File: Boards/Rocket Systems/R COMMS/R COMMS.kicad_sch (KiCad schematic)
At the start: 47 parts, among them IC1 NSVT30010MXV6T1G, IC2 NSVT30010MXV6T1G, J2 22022065, J4 MEM2061-01-188-00-A_REVA, J6 SMA_CONNECTOR, J7 SMA_CONNECTOR, J9 Conn_01x04_Socket, U3 SX1280IMLTRT, U4 NRF21540-QDAA-R, U6 MAX485CSA+T

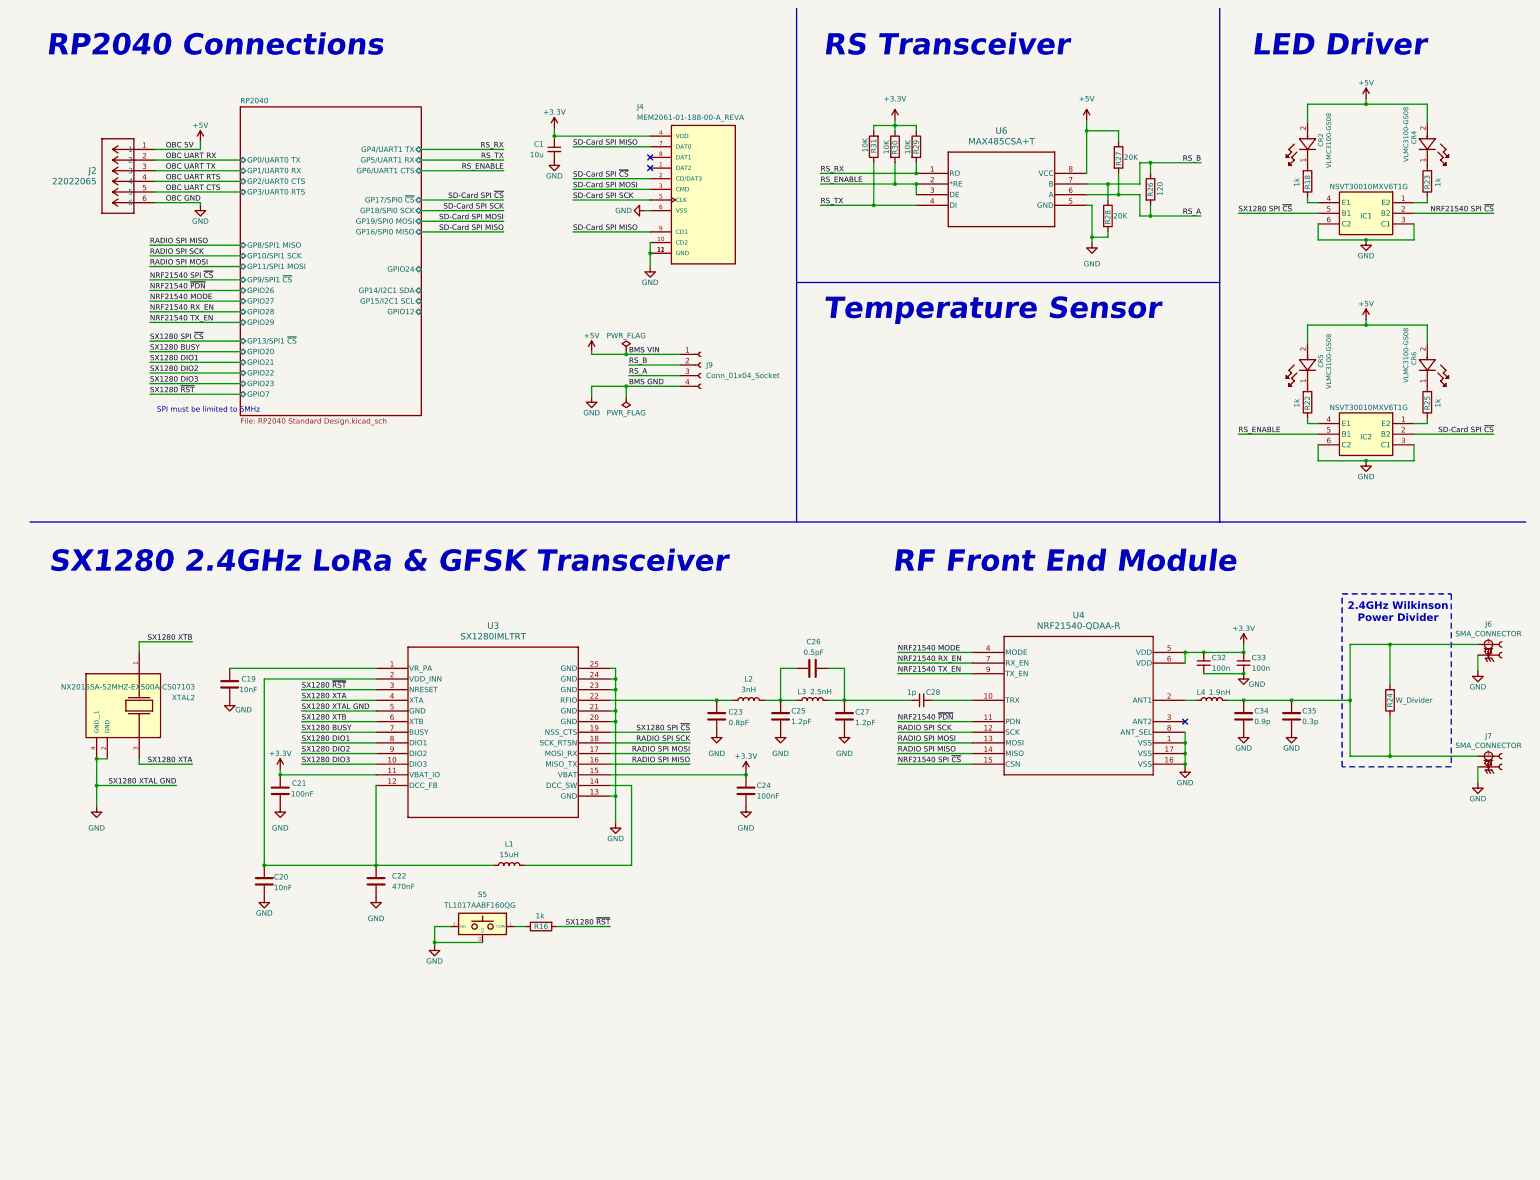
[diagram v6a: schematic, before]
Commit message: Communication System final Schematic Update
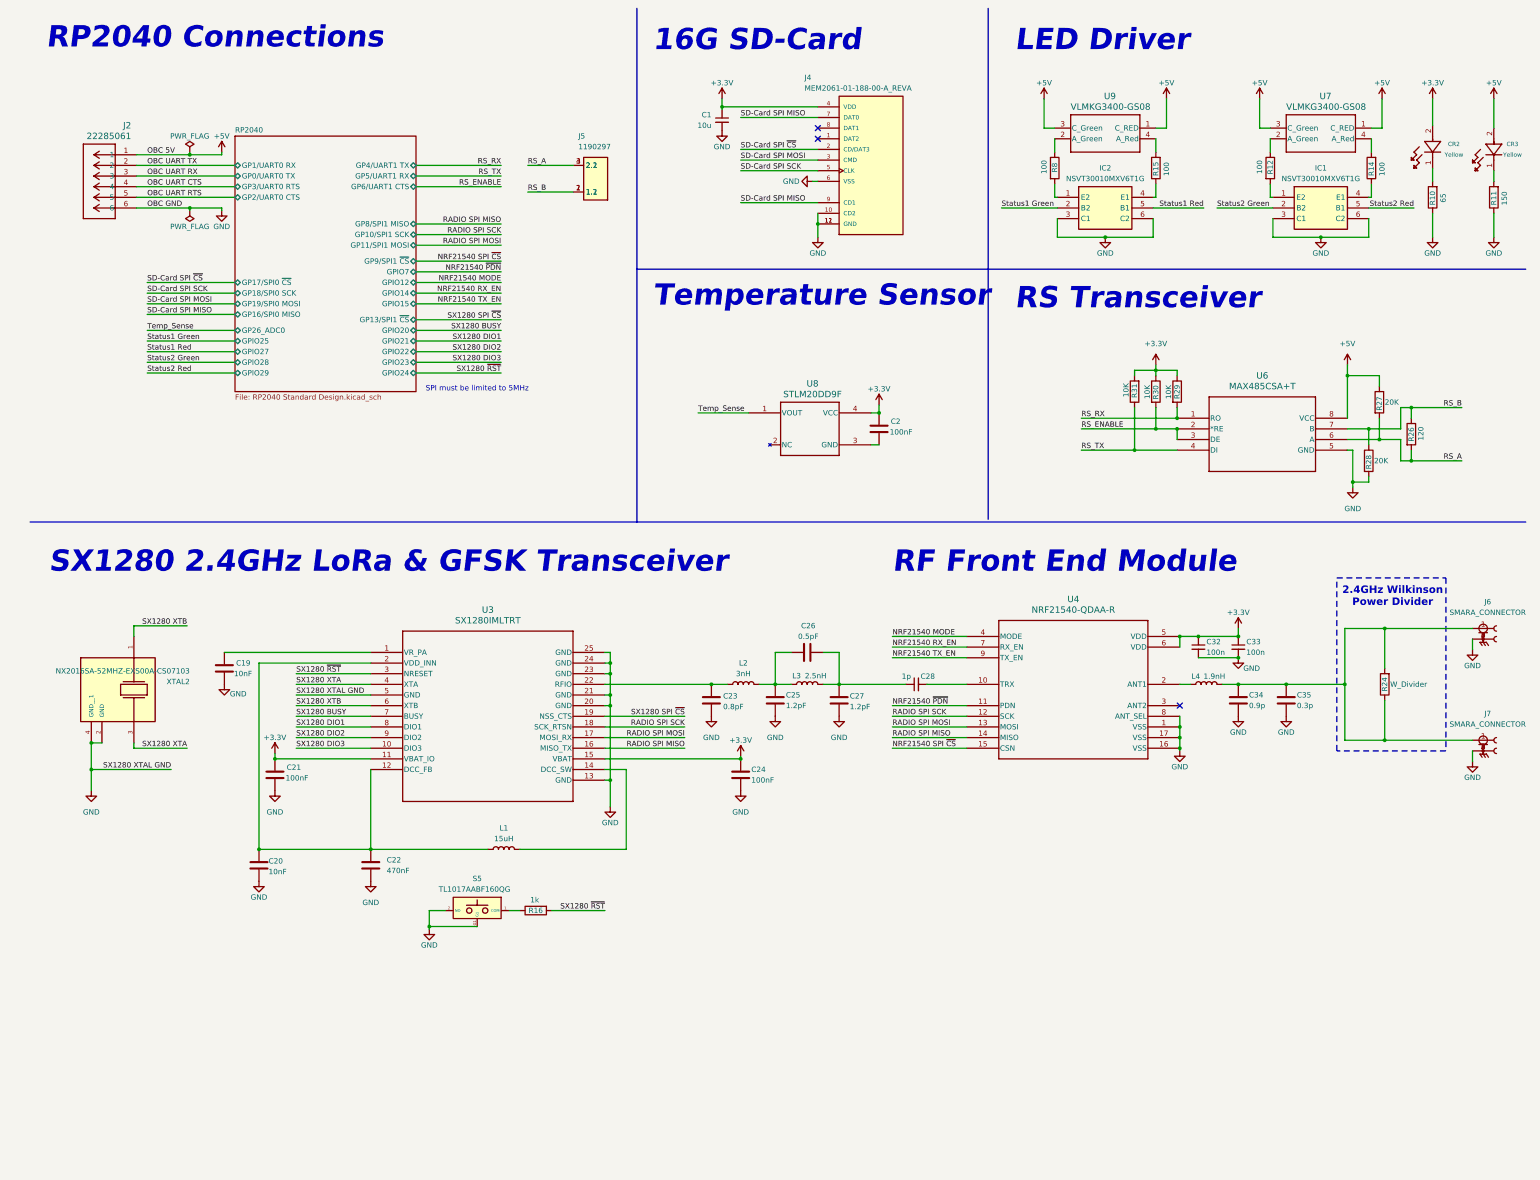
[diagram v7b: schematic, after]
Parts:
- removed CR2, CR4, CR5, CR6: VLMC3100-GS08, LED-Green_VLMC3100-GS08:LED_PLCC_VSMB, symbol GreenLED__VLMC3100-GS08:VLMC3100-GS08
- removed J2: 22022065, CONN_SA-4455_06_TE_MOL, symbol CONN_SA-4455_06_TE_MOL:22022065
- removed J6: SMA_CONNECTOR, SMA_CONNECTOR:LPRS_SMA_CONNECTOR, symbol SMA_CONNECTOR:SMA_CONNECTOR
- removed J7: SMA_CONNECTOR, Inductor-0805:Inductor_0805, symbol SMA_CONNECTOR:SMA_CONNECTOR
- removed J9: Conn_01x04_Socket, symbol Connector:Conn_01x04_Socket
- removed R18, R22, R23, R25: 1k, Resistor-0402:RES_0402, symbol Device:R
- added C2: 100nF, Capacitor-0402:Capacitor_0402, symbol Device:C
- added CR2, CR3: VLMY1300-GS08, LED-Yellow_VLMY1300-GS08:LED_VISHAY_VLMX1300_VIS, symbol VLMY1300-GS08:VLMY1300-GS08
- added J2: 22285061, CONN Male Header:CONN_SD-42375-001_M320_06_MOL, symbol PinCon_22285061:22285061
- added J5: 1190297, LPT Conn 2 Entradas:1190297, symbol 1190297:1190297
- added J6, J7: SMARA_CONNECTOR, SMARACONNECTOR, symbol SMARA_CONNECTOR:SMARA_CONNECTOR
- added R10: 65, Resistor-0402:RES_0402, symbol Device:R
- added R11: 150, Resistor-0402:RES_0402, symbol Device:R
- added R12, R14, R15, R8: 100, Resistor-0402:RES_0402, symbol Device:R
- added U7, U9: VLMKG3400-GS08, VLMKG3400-GS08:SMT_00-GS08_VIS, symbol VLMKG3400-GS08:VLMKG3400-GS08
- added U8: STLM20DD9F, STLM20DD9F:UDFN-4L_STM, symbol STLM20DD9F:STLM20DD9F
- C1: footprint (none) -> Capacitor-0805:Capacitor_0805
- IC1, IC2: footprint 2 PNP:SOTFL50P160X60-6N -> 2 PNP:SOT-563_1P3X1P7_ONS
- J4: footprint MEM2061-01-188-00-A_REVA:GCT_MEM2061-01-188-00-A_REVA -> SD-CARD_MEM2061-01-188-00-A:GCT_MEM2061-01-188-00-A_REVA
- L1: footprint Inductor-0805:IND_15uH_0805 -> Inductor-0805:Inductor_0805
- R24: footprint Resistor-0805:R_0805_5K1 -> Resistor-0805:RES_0805
- S5: footprint TL1017AABF160QG -> E-Switch_Small:TL1017AABF160QG
- U3: footprint QFN24_4X4_SEM -> SX1280:QFN24_4X4_SEM
- U4: footprint QFN16_4X4_NOR -> RF FEM:QFN16_4X4_NOR
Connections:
- net +3.3V: now also C2.1, CR2.2, U8.4 (VCC)
- net +5V: now also CR3.2, J2.1, U7.1 (C_RED), U7.3 (C_Green), U9.1 (C_RED), U9.3 (C_Green)
- net GND: now also J2.6, J6.2, J6.3, J6.4, J6.5, J7.2, J7.3, J7.4, J7.5, R10.1, R11.1
- net NRF21540 SPI ~{CS}: no longer IC1.2 (B2)
- net OBC UART CTS: now also J2.4
- net OBC UART RTS: now also J2.5
- net OBC UART RX: now also J2.3
- net OBC UART TX: now also J2.2
- net RS_A: now also J5.3 (2.1), J5.4 (2.2)
- net RS_B: now also J5.1 (1.1), J5.2 (1.2)
- net RS_ENABLE: no longer IC2.5 (B1)
- net SD-Card SPI ~{CS}: no longer IC2.2 (B2)
- net SX1280 SPI ~{CS}: no longer IC1.5 (B1)
- net at IC1.1 (E2): now also R12.2
- net at IC1.4 (E1): now also R14.1
- net at IC2.1 (E2): now also R8.2
- net at IC2.4 (E1): now also R15.1
- net at C34.1, C35.1, L4.2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: now also J6.1, J7.1
- new net: CR2.1, R10.2
- new net: CR3.1, R11.2
- new net: R12.1, U7.2 (A_Green)
- new net: R14.2, U7.4 (A_Red)
- new net: R8.1, U9.2 (A_Green)
- new net: C2.2, U8.3 (GND)
- new net: R15.2, U9.4 (A_Red)
- new net Status1 Green: IC2.2 (B2)
- new net Status1 Red: IC2.5 (B1)
- new net Status2 Green: IC1.2 (B2)
- new net Status2 Red: IC1.5 (B1)
- new net Temp_Sense: U8.1 (VOUT)
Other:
- sheet RP2040 ports: added GP26_ADC0, GPIO14, GPIO15, GPIO25; removed GP14/I2C1 SDA, GP15/I2C1 SCL, GPIO26
- note added: "16G SD-Card"
- moved on the sheet: C1, C19, C20, C21, C22, C23, C24, C25, C26, C27, C28, C32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

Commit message: Development board update
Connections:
- net GND: now also J4.9 (CD1)
- net SD-Card SPI MISO: no longer J4.9 (CD1)
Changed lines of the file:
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@@
 	)
 	(junction
+		(at 200.025 60.96)
+		(diameter 0)
+		(color 0 0 0 0)
+	)
+	(junction
 		(at 326.39 99.695)
 		(diameter 0)
@@
 		(color 0 0 0 0)
 	)
+	(junction
+		(at 200.025 58.42)
+		(diameter 0)
+		(color 0 0 0 0)
+	)
 	(no_connect
 		(at 200.025 40.64)
@@
 	(wire
 		(pts
-			(xy 198.755 53.34) (xy 200.025 53.34)
-		)
-		(stroke
-			(width 0)
-			(type default)
-		)
-	)
-	(wire
-		(pts
 			(xy 341.63 107.315) (xy 341.63 109.855)
 		)
@@
 	(wire
 		(pts
-			(xy 181.61 58.42) (xy 200.025 58.42)
-		)
-		(stroke
-			(width 0)
-			(type default)
-		)
-	)
-	(wire
-		(pts
 			(xy 280.67 107.315) (xy 280.67 112.395)
 		)
@@
 	(wire
 		(pts
+			(xy 200.025 58.42) (xy 200.025 60.96)
+		)
+		(stroke
+			(width 0)
+			(type default)
+		)
+	)
+	(wire
+		(pts
 			(xy 339.09 120.015) (xy 341.63 120.015)
 		)
@@
 	(wire
 		(pts
+			(xy 200.025 53.34) (xy 200.025 58.42)
+		)
+		(stroke
+			(width 0)
+			(type default)
+		)
+	)
+	(wire
+		(pts
 			(xy 37.465 49.53) (xy 60.96 49.53)
 		)
@@
 		)
 	)
-	(label "SD-Card SPI MISO"
-		(at 181.61 58.42 0)
-		(effects
-			(font
-				(size 1.27 1.27)
-			)
-			(justify left bottom)
-		)
-	)
 	(label "RS_TX"
 		(at 262.89 117.475 0)
@@
 					(unit 1)
 				)
-			)
-		)
-	)
-	(symbol
-		(lib_id "power:GND")
-		(at 198.755 53.34 270)
-		(unit 1)
-		(exclude_from_sim no)
-		(in_bom yes)
-		(on_board yes)
-		(dnp no)
-		(property "Reference" "#PWR069"
-			(at 192.405 53.34 0)
-			(effects
-				(font
-					(size 1.27 1.27)
-				)
-				(hide yes)
-			)
-		)
-		(property "Value" "GND"
-			(at 193.675 53.34 90)
-			(effects
-				(font
-					(size 1.27 1.27)
-				)
-			)
-		)
-		(property "Footprint" ""
-			(at 198.755 53.34 0)
-			(effects
-				(font
-					(size 1.27 1.27)
-				)
-				(hide yes)
-			)
-		)
-		(property "Datasheet" ""
-			(at 198.755 53.34 0)
-			(effects
-				(font
-					(size 1.27 1.27)
-				)
-				(hide yes)
-			)
-		)
-		(property "Description" "Power symbol creates a global label with name \"GND\" , ground"
-			(at 198.755 53.34 0)
-			(effects
-				(font
-					(size 1.27 1.27)
-				)
-				(hide yes)
-			)
-		)
-		(pin "1"
-		)
-		(instances
-			(project "R COMMS"
-				(path "/169b1789-9bea-4709-830d-1c7983087293"
-					(reference "#PWR069")
-					(unit 1)
-				)
